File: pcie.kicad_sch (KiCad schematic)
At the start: 25 parts, among them J10 OCuLink_x4_Amphenol_G14A42121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, J11 OCuLink_x4_Amphenol_G14A42121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, J17 PinHeader_2x10_P1.27mm_SMD_Sh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

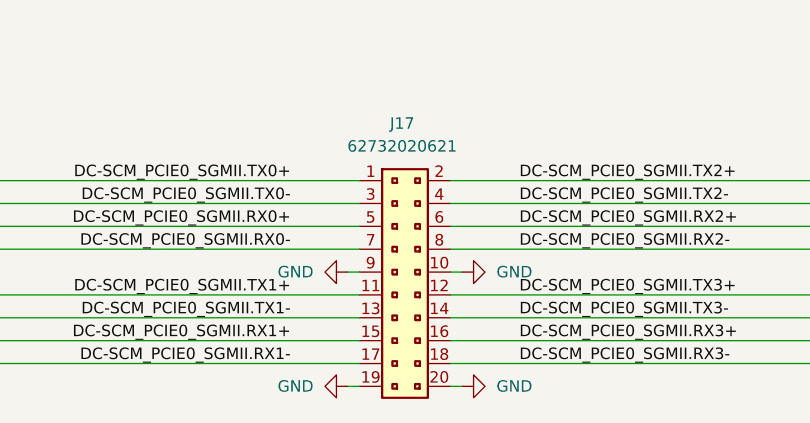
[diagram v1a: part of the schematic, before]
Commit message: [#93514] Add dnp to PCIE components testpads
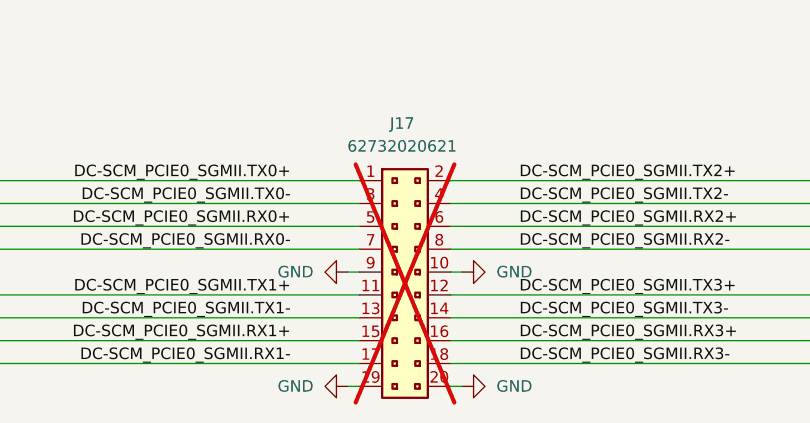
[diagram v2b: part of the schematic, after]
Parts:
- J17: now not fitted
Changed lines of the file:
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@@
 		(in_bom yes)
 		(on_board yes)
-		(dnp no)
+		(dnp yes)
 		(fields_autoplaced yes)
 		(property "Reference" "J17"

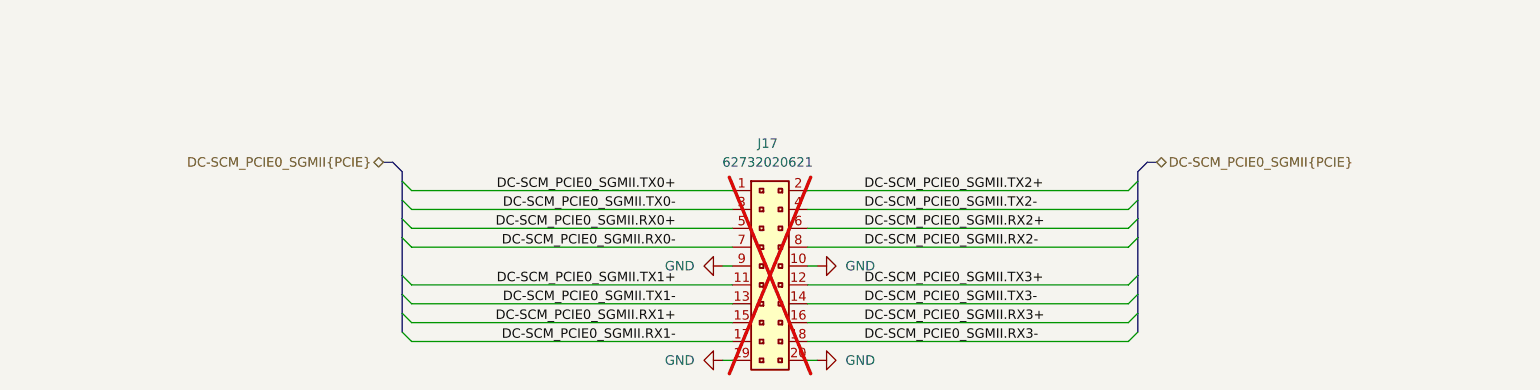
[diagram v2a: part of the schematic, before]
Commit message: [#93514] Remove unnecessary PCIE testpads
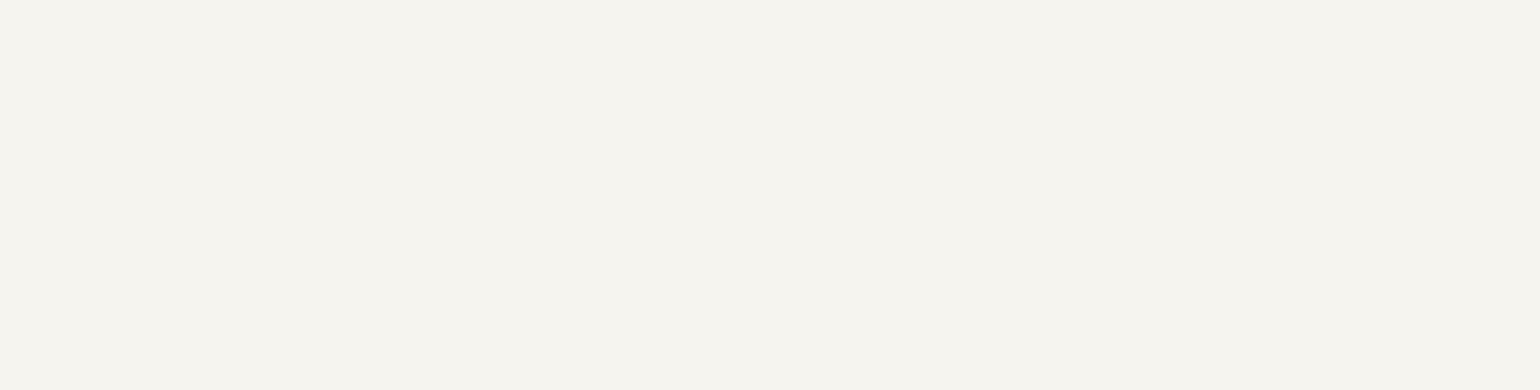
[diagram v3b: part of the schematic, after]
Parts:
- removed J17: PinHeader_2x10_P1.27mm_SMD_Shrouded, antmicro-footprints:PinHeader_2x10_P1.27mm_SMD_Shrouded, symbol antmicroGenericPinHeaders:PinHeader_2x10_P1.27mm_SMD_Shrouded

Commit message: [#93514] Add 2 TVS diodes for PCIE
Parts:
- added D13, D9: ESD204DQAR, antmicro-footprints:USON-10_2.5x1mm_P0.5mm, symbol antmicroTVSDiodes:ESD204DQAR
- renumbered D8 to D12, D9 to D8
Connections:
- net DC-SCM_PCIE1.TX0+: now also D9.1, D9.10; no longer D8.4, D8.7
- net DC-SCM_PCIE1.TX0-: now also D9.2, D9.9; no longer D8.5, D8.6
- net DC-SCM_PCIE_USB_SCMROOT.RX0+: now also D13.1, D13.10; no longer D12.4, D12.7
- net DC-SCM_PCIE_USB_SCMROOT.RX0-: now also D13.2, D13.9; no longer D12.5, D12.6
- net GND: now also D13.3, D13.8, D9.3, D9.8
- new net: D13.4, D13.7
- new net: D13.5, D13.6
- new net: D9.4, D9.7
- new net: D9.5, D9.6
- new net: D12.4, D12.7
- new net: D12.5, D12.6
- new net: D8.4, D8.7
- new net: D8.5, D8.6
- no-connect marks 26 -> 34
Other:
- moved on the sheet: D8

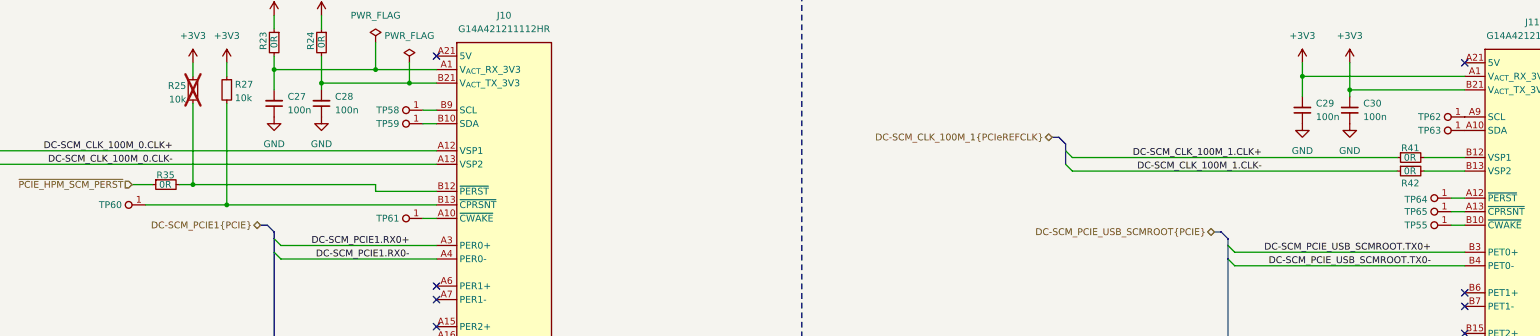
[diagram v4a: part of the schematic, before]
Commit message: [#93949] Change testpads to 1.5mm, change QSPI and UART testpad to smd technology
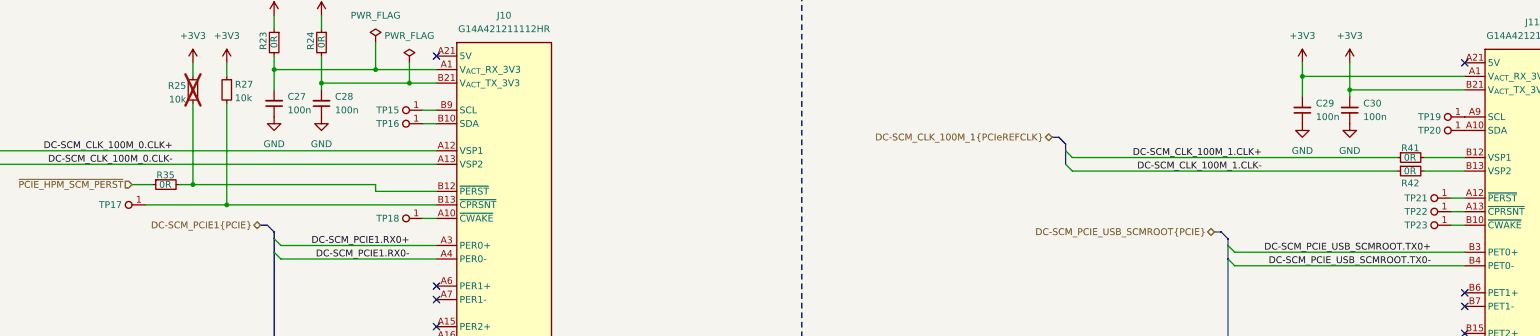
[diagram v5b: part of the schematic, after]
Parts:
- removed TP55, TP58, TP59, TP60, TP61, TP62, TP63, TP64, TP65: TP_0.75mm_SMD, antmicro-footprints:TP_SMD_0.75mm, symbol antmicroTestPoints:TP_0.75mm_SMD
- added TP15, TP16, TP17, TP18, TP19, TP20, TP21, TP22, TP23: TP_1.5mm_SMD, antmicro-footprints:TP_SMD_1.5mm, symbol antmicroTestPoints:TP_1.5mm_SMD
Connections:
- net at J11.A10 (SDA): now also TP20.1
- net at J11.A12 (~{PERST}): now also TP21.1
- net at J11.A13 (~{CPRSNT}): now also TP22.1
- net at J11.A9 (SCL): now also TP19.1
- net at J11.B10 (~{CWAKE}): now also TP23.1
- net at J10.A10 (~{CWAKE}): now also TP18.1
- net at J10.B10 (SDA): now also TP16.1
- net at J10.B13 (~{CPRSNT}), R27.2: now also TP17.1
- net at J10.B9 (SCL): now also TP15.1

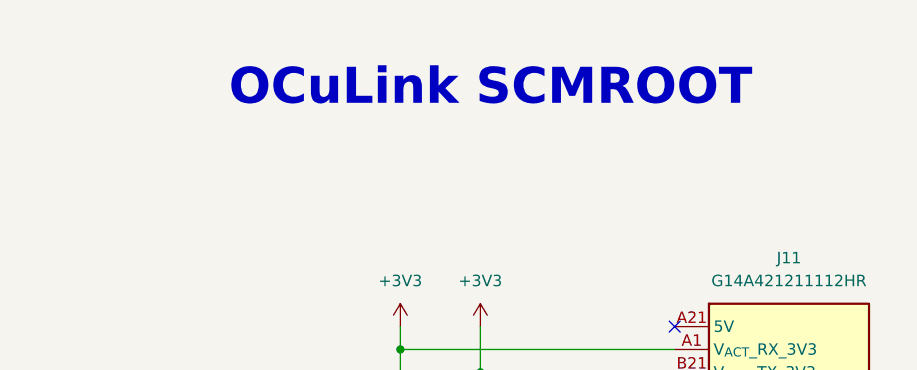
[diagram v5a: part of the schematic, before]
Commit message: [#93949] Align items to grid, change TP for UART
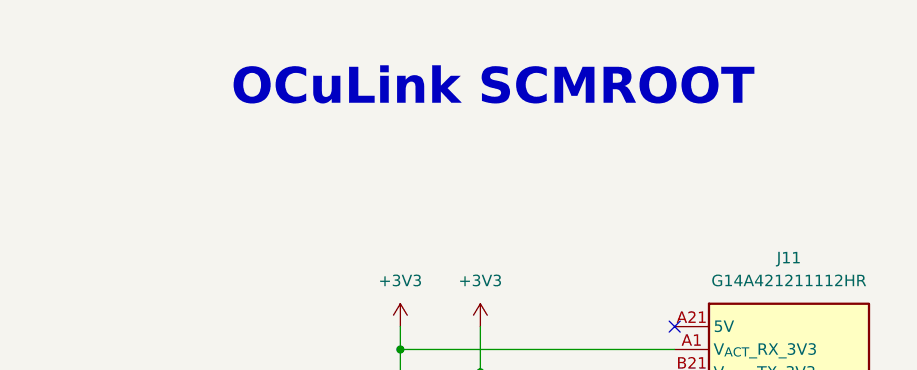
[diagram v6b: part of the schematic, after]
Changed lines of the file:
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@@
 	(text "OCuLink SCMROOT\n"
 		(exclude_from_sim no)
-		(at 342.646 22.86 0)
+		(at 342.9 22.86 0)
 		(effects
 			(font

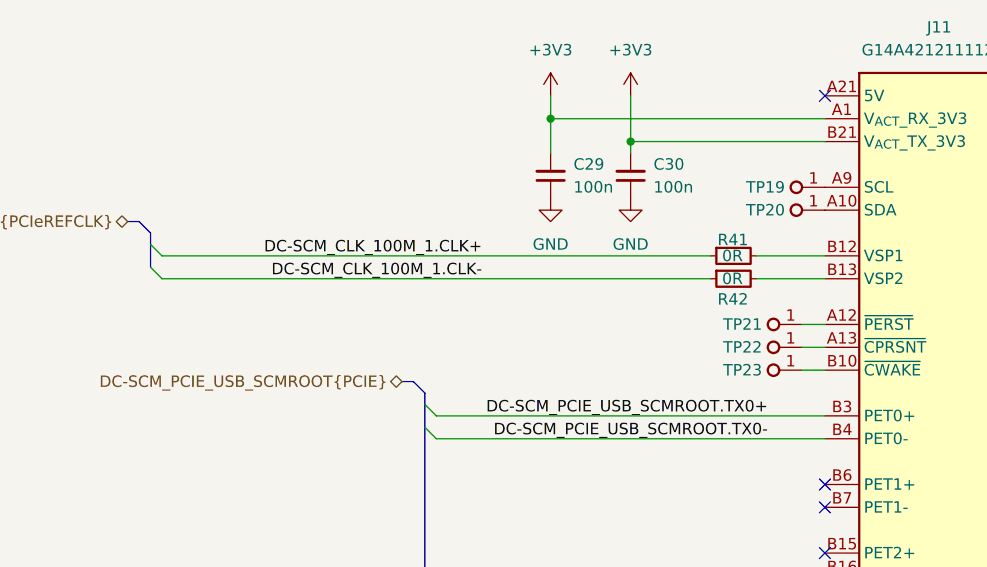
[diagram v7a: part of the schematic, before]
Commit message: [#94820] Route PCIE clocks as diff pair
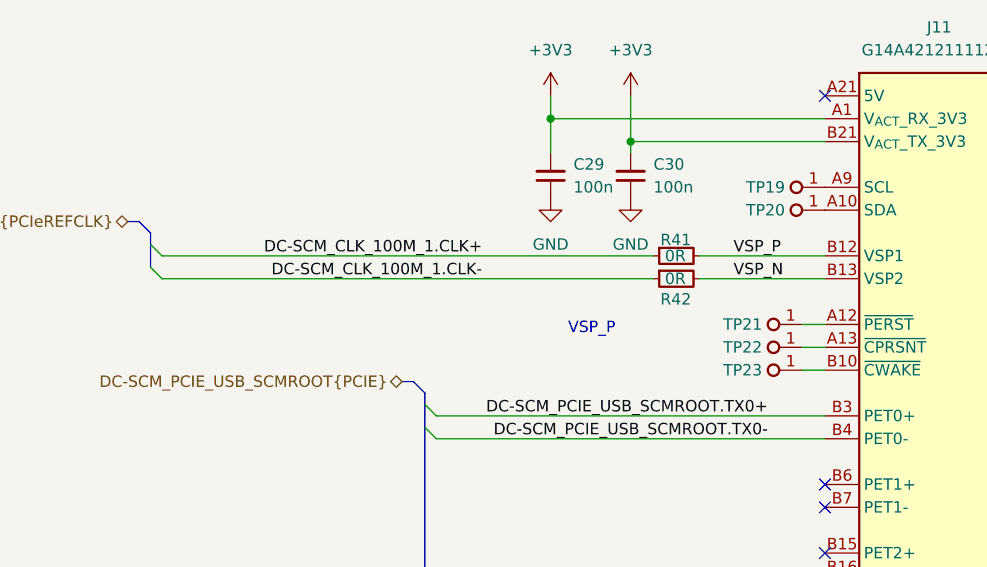
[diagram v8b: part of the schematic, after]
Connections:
- net VSP_P: now reaches J11.B12 (VSP1), R41.2
- net VSP_N: now reaches J11.B13 (VSP2), R42.2
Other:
- note added: "VSP_P"
- moved on the sheet: R41, R42
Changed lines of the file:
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@@
 		)
 	)
+	(text "VSP_P"
+		(exclude_from_sim no)
+		(at 308.102 72.898 0)
+		(effects
+			(font
+				(size 1.27 1.27)
+			)
+		)
+	)
 	(text "OCuLink SCMROOT\n"
 		(exclude_from_sim no)
@@
 	(wire
 		(pts
-			(xy 260.35 67.31) (xy 321.31 67.31)
+			(xy 260.35 67.31) (xy 314.96 67.31)
 		)
 		(stroke
@@
 	(wire
 		(pts
-			(xy 326.39 67.31) (xy 334.01 67.31)
+			(xy 320.04 67.31) (xy 334.01 67.31)
 		)
 		(stroke
@@
 	(wire
 		(pts
-			(xy 260.35 64.77) (xy 321.31 64.77)
+			(xy 260.35 64.77) (xy 314.96 64.77)
 		)
 		(stroke
@@
 	(wire
 		(pts
-			(xy 326.39 64.77) (xy 334.01 64.77)
+			(xy 320.04 64.77) (xy 334.01 64.77)
 		)
 		(stroke
@@
 		)
 	)
+	(label "VSP_P"
+		(at 323.85 64.77 0)
+		(effects
+			(font
+				(size 1.27 1.27)
+			)
+			(justify left bottom)
+		)
+	)
 	(label "DC-SCM_PCIE_USB_SCMROOT.TX0-"
 		(at 332.74 177.8 180)
@@
 		)
 	)
+	(label "VSP_N"
+		(at 323.85 67.31 0)
+		(effects
+			(font
+				(size 1.27 1.27)
+			)
+			(justify left bottom)
+		)
+	)
 	(hierarchical_label "DC-SCM_PCIE1{PCIE}"
 		(shape bidirectional)
@@
 		(lib_name "R_0R_0402_1")
 		(lib_id "antmicroResistors0402:R_0R_0402")
-		(at 321.31 67.31 0)
+		(at 314.96 67.31 0)
 		(unit 1)
 		(exclude_from_sim no)
@@
 		(dnp no)
 		(property "Reference" "R42"
-			(at 322.072 69.596 0)
+			(at 315.722 69.596 0)
 			(effects
 				(font
@@
 		)
 		(property "Value" "R_0R_0402"
-			(at 341.63 80.01 0)
+			(at 335.28 80.01 0)
 			(effects
 				(font
@@
 		)
 		(property "Footprint" "antmicro-footprints:R_0402_1005Metric"
-			(at 341.63 82.55 0)
+			(at 335.28 82.55 0)
 			(effects
 				(font
@@
 		)
 		(property "Datasheet" "https://industrial.panasonic.com/cdbs/www-data/pdf/RDA0000/AOA0000C301.pdf"
-			(at 341.63 85.09 0)
+			(at 335.28 85.09 0)
 			(effects
 				(font
@@
 		)
 		(property "Description" "SMD Chip Resistor, Jumper, 0 ohm, 100 mW, 0402 [1005 Metric], Thick Film, General Purpose"
-			(at 341.63 100.33 0)
+			(at 335.28 100.33 0)
 			(effects
 				(font
@@
 		)
 		(property "MPN" "ERJ2GE0R00X"
-			(at 341.63 87.63 0)
+			(at 335.28 87.63 0)
 			(effects
 				(font
@@
 		)
 		(property "Manufacturer" "Panasonic"
-			(at 341.63 90.17 0)
+			(at 335.28 90.17 0)
 			(effects
 				(font
@@
 		)
 		(property "License" "Apache-2.0"
-			(at 341.63 92.71 0)
+			(at 335.28 92.71 0)
 			(effects
 				(font
@@
 		)
 		(property "Author" "Antmicro"
-			(at 341.63 95.25 0)
+			(at 335.28 95.25 0)
 			(effects
 				(font
@@
 		)
 		(property "Val" "0R"
-			(at 322.58 67.31 0)
+			(at 316.23 67.31 0)
 			(effects
 				(font
@@
 		)
 		(property "Tolerance" "~"
-			(at 341.63 77.47 0)
+			(at 335.28 77.47 0)
 			(effects
 				(font
@@
 		)
 		(property "Current" "1A"
-			(at 341.63 97.79 0)
+			(at 335.28 97.79 0)
 			(effects
 				(font
@@
 		(lib_name "R_0R_0402_1")
 		(lib_id "antmicroResistors0402:R_0R_0402")
-		(at 321.31 64.77 0)
+		(at 314.96 64.77 0)
 		(unit 1)
 		(exclude_from_sim no)
@@
 		(dnp no)
 		(property "Reference" "R41"
-			(at 322.072 62.992 0)
+			(at 315.722 62.992 0)
 			(effects
 				(font
@@
 		)
 		(property "Value" "R_0R_0402"
-			(at 341.63 77.47 0)
+			(at 335.28 77.47 0)
 			(effects
 				(font
@@
 		)
 		(property "Footprint" "antmicro-footprints:R_0402_1005Metric"
-			(at 341.63 80.01 0)
+			(at 335.28 80.01 0)
 			(effects
 				(font
@@
 		)
 		(property "Datasheet" "https://industrial.panasonic.com/cdbs/www-data/pdf/RDA0000/AOA0000C301.pdf"
-			(at 341.63 82.55 0)
+			(at 335.28 82.55 0)
 			(effects
 				(font
@@
 		)
 		(property "Description" "SMD Chip Resistor, Jumper, 0 ohm, 100 mW, 0402 [1005 Metric], Thick Film, General Purpose"
-			(at 341.63 97.79 0)
+			(at 335.28 97.79 0)
 			(effects
 				(font
@@
 		)
 		(property "MPN" "ERJ2GE0R00X"
-			(at 341.63 85.09 0)
+			(at 335.28 85.09 0)
 			(effects
 				(font
@@
 		)
 		(property "Manufacturer" "Panasonic"
-			(at 341.63 87.63 0)
+			(at 335.28 87.63 0)
 			(effects
 				(font
@@
 		)
 		(property "License" "Apache-2.0"
-			(at 341.63 90.17 0)
+			(at 335.28 90.17 0)
 			(effects
 				(font
@@
 		)
 		(property "Author" "Antmicro"
-			(at 341.63 92.71 0)
+			(at 335.28 92.71 0)
 			(effects
 				(font
@@
 		)
 		(property "Val" "0R"
-			(at 322.58 64.77 0)
+			(at 316.23 64.77 0)
 			(effects
 				(font
@@
 		)
 		(property "Tolerance" "~"
-			(at 341.63 74.93 0)
+			(at 335.28 74.93 0)
 			(effects
 				(font
@@
 		)
 		(property "Current" "1A"
-			(at 341.63 95.25 0)
+			(at 335.28 95.25 0)
 			(effects
 				(font
